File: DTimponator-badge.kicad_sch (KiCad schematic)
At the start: 29 parts, among them J1 AVR-ISP, SW1 SW_SPDT, SW2 SW_Push, SW3 SW_Push, U1 ATtiny84A-SS

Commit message: Changed much to SMD
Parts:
- C1: footprint Capacitor_THT:C_Disc_D5.0mm_W2.5mm_P5.00mm -> Capacitor_SMD:C_1206_3216Metric_Pad1.33x1.80mm_HandSolder
- J1: footprint Connector_IDC:IDC-Header_2x03_P2.54mm_Vertical -> Connector_PinHeader_2.54mm:PinHeader_2x03_P2.54mm_Vertical_SMD
- R1, R2, R3, R4, R5, R6: footprint Resistor_THT:R_Axial_DIN0207_L6.3mm_D2.5mm_P7.62mm_Horizontal -> Resistor_SMD:R_0805_2012Metric_Pad1.20x1.40mm_HandSolder
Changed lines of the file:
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@@
     (property "Reference" "R1" (id 0) (at 41.91 83.6422 90))
     (property "Value" "330" (id 1) (at 41.91 85.9536 90))
-    (property "Footprint" "Resistor_THT:R_Axial_DIN0207_L6.3mm_D2.5mm_P7.62mm_Horizontal" (id 2) (at 41.91 87.122 90)
+    (property "Footprint" "Resistor_SMD:R_0805_2012Metric_Pad1.20x1.40mm_HandSolder" (id 2) (at 41.91 87.122 90)
       (effects (font (size 1.27 1.27)) hide)
     )
@@
     (property "Reference" "R2" (id 0) (at 41.91 109.0422 90))
     (property "Value" "330" (id 1) (at 41.91 111.3536 90))
-    (property "Footprint" "Resistor_THT:R_Axial_DIN0207_L6.3mm_D2.5mm_P7.62mm_Horizontal" (id 2) (at 41.91 112.522 90)
+    (property "Footprint" "Resistor_SMD:R_0805_2012Metric_Pad1.20x1.40mm_HandSolder" (id 2) (at 41.91 112.522 90)
       (effects (font (size 1.27 1.27)) hide)
     )
@@
     (property "Reference" "R3" (id 0) (at 41.91 134.4422 90))
     (property "Value" "330" (id 1) (at 41.91 136.7536 90))
-    (property "Footprint" "Resistor_THT:R_Axial_DIN0207_L6.3mm_D2.5mm_P7.62mm_Horizontal" (id 2) (at 41.91 137.922 90)
+    (property "Footprint" "Resistor_SMD:R_0805_2012Metric_Pad1.20x1.40mm_HandSolder" (id 2) (at 41.91 137.922 90)
       (effects (font (size 1.27 1.27)) hide)
     )
@@
     (property "Reference" "R4" (id 0) (at 41.91 159.8422 90))
     (property "Value" "330" (id 1) (at 41.91 162.1536 90))
-    (property "Footprint" "Resistor_THT:R_Axial_DIN0207_L6.3mm_D2.5mm_P7.62mm_Horizontal" (id 2) (at 41.91 163.322 90)
+    (property "Footprint" "Resistor_SMD:R_0805_2012Metric_Pad1.20x1.40mm_HandSolder" (id 2) (at 41.91 163.322 90)
       (effects (font (size 1.27 1.27)) hide)
     )
@@
       (effects (font (size 1.27 1.27)) (justify right))
     )
-    (property "Footprint" "Connector_IDC:IDC-Header_2x03_P2.54mm_Vertical" (id 2) (at 257.81 54.61 90)
+    (property "Footprint" "Connector_PinHeader_2.54mm:PinHeader_2x03_P2.54mm_Vertical_SMD" (id 2) (at 257.81 54.61 90)
       (effects (font (size 1.27 1.27)) hide)
     )
@@
     (property "Reference" "R5" (id 0) (at 156.21 70.9422 90))
     (property "Value" "10k" (id 1) (at 156.21 73.2536 90))
-    (property "Footprint" "Resistor_THT:R_Axial_DIN0207_L6.3mm_D2.5mm_P7.62mm_Horizontal" (id 2) (at 156.21 74.422 90)
+    (property "Footprint" "Resistor_SMD:R_0805_2012Metric_Pad1.20x1.40mm_HandSolder" (id 2) (at 156.21 74.422 90)
       (effects (font (size 1.27 1.27)) hide)
     )
@@
     (property "Reference" "R6" (id 0) (at 194.31 70.9422 90))
     (property "Value" "10k" (id 1) (at 194.31 73.2536 90))
-    (property "Footprint" "Resistor_THT:R_Axial_DIN0207_L6.3mm_D2.5mm_P7.62mm_Horizontal" (id 2) (at 194.31 74.422 90)
+    (property "Footprint" "Resistor_SMD:R_0805_2012Metric_Pad1.20x1.40mm_HandSolder" (id 2) (at 194.31 74.422 90)
       (effects (font (size 1.27 1.27)) hide)
     )
@@
       (effects (font (size 1.27 1.27)) (justify left))
     )
-    (property "Footprint" "Capacitor_THT:C_Disc_D5.0mm_W2.5mm_P5.00mm" (id 2) (at 73.3552 49.53 0)
+    (property "Footprint" "Capacitor_SMD:C_1206_3216Metric_Pad1.33x1.80mm_HandSolder" (id 2) (at 73.3552 49.53 0)
       (effects (font (size 1.27 1.27)) hide)
     )
@@
     )
     (path "/00000000-0000-0000-0000-0000601b337a"
-      (reference "C1") (unit 1) (value ".1uF") (footprint "Capacitor_THT:C_Disc_D5.0mm_W2.5mm_P5.00mm")
+      (reference "C1") (unit 1) (value ".1uF") (footprint "Capacitor_SMD:C_1206_3216Metric_Pad1.33x1.80mm_HandSolder")
     )
     (path "/00000000-0000-0000-0000-00005fc12c5a"
@@
     )
     (path "/00000000-0000-0000-0000-00005fcd6c92"
-      (reference "J1") (unit 1) (value "AVR-ISP") (footprint "Connector_IDC:IDC-Header_2x03_P2.54mm_Vertical")
+      (reference "J1") (unit 1) (value "AVR-ISP") (footprint "Connector_PinHeader_2.54mm:PinHeader_2x03_P2.54mm_Vertical_SMD")
     )
     (path "/00000000-0000-0000-0000-00005fc55ab2"
-      (reference "R1") (unit 1) (value "330") (footprint "Resistor_THT:R_Axial_DIN0207_L6.3mm_D2.5mm_P7.62mm_Horizontal")
+      (reference "R1") (unit 1) (value "330") (footprint "Resistor_SMD:R_0805_2012Metric_Pad1.20x1.40mm_HandSolder")
     )
     (path "/00000000-0000-0000-0000-00005fc7641b"
-      (reference "R2") (unit 1) (value "330") (footprint "Resistor_THT:R_Axial_DIN0207_L6.3mm_D2.5mm_P7.62mm_Horizontal")
+      (reference "R2") (unit 1) (value "330") (footprint "Resistor_SMD:R_0805_2012Metric_Pad1.20x1.40mm_HandSolder")
     )
     (path "/00000000-0000-0000-0000-00005fc76f9f"
-      (reference "R3") (unit 1) (value "330") (footprint "Resistor_THT:R_Axial_DIN0207_L6.3mm_D2.5mm_P7.62mm_Horizontal")
+      (reference "R3") (unit 1) (value "330") (footprint "Resistor_SMD:R_0805_2012Metric_Pad1.20x1.40mm_HandSolder")
     )
     (path "/00000000-0000-0000-0000-00005fc772c9"
-      (reference "R4") (unit 1) (value "330") (footprint "Resistor_THT:R_Axial_DIN0207_L6.3mm_D2.5mm_P7.62mm_Horizontal")
+      (reference "R4") (unit 1) (value "330") (footprint "Resistor_SMD:R_0805_2012Metric_Pad1.20x1.40mm_HandSolder")
     )
     (path "/00000000-0000-0000-0000-00005fdaba63"
-      (reference "R5") (unit 1) (value "10k") (footprint "Resistor_THT:R_Axial_DIN0207_L6.3mm_D2.5mm_P7.62mm_Horizontal")
+      (reference "R5") (unit 1) (value "10k") (footprint "Resistor_SMD:R_0805_2012Metric_Pad1.20x1.40mm_HandSolder")
     )
     (path "/00000000-0000-0000-0000-00005fdaccd5"
-      (reference "R6") (unit 1) (value "10k") (footprint "Resistor_THT:R_Axial_DIN0207_L6.3mm_D2.5mm_P7.62mm_Horizontal")
+      (reference "R6") (unit 1) (value "10k") (footprint "Resistor_SMD:R_0805_2012Metric_Pad1.20x1.40mm_HandSolder")
     )
     (path "/00000000-0000-0000-0000-00005fcb2142"

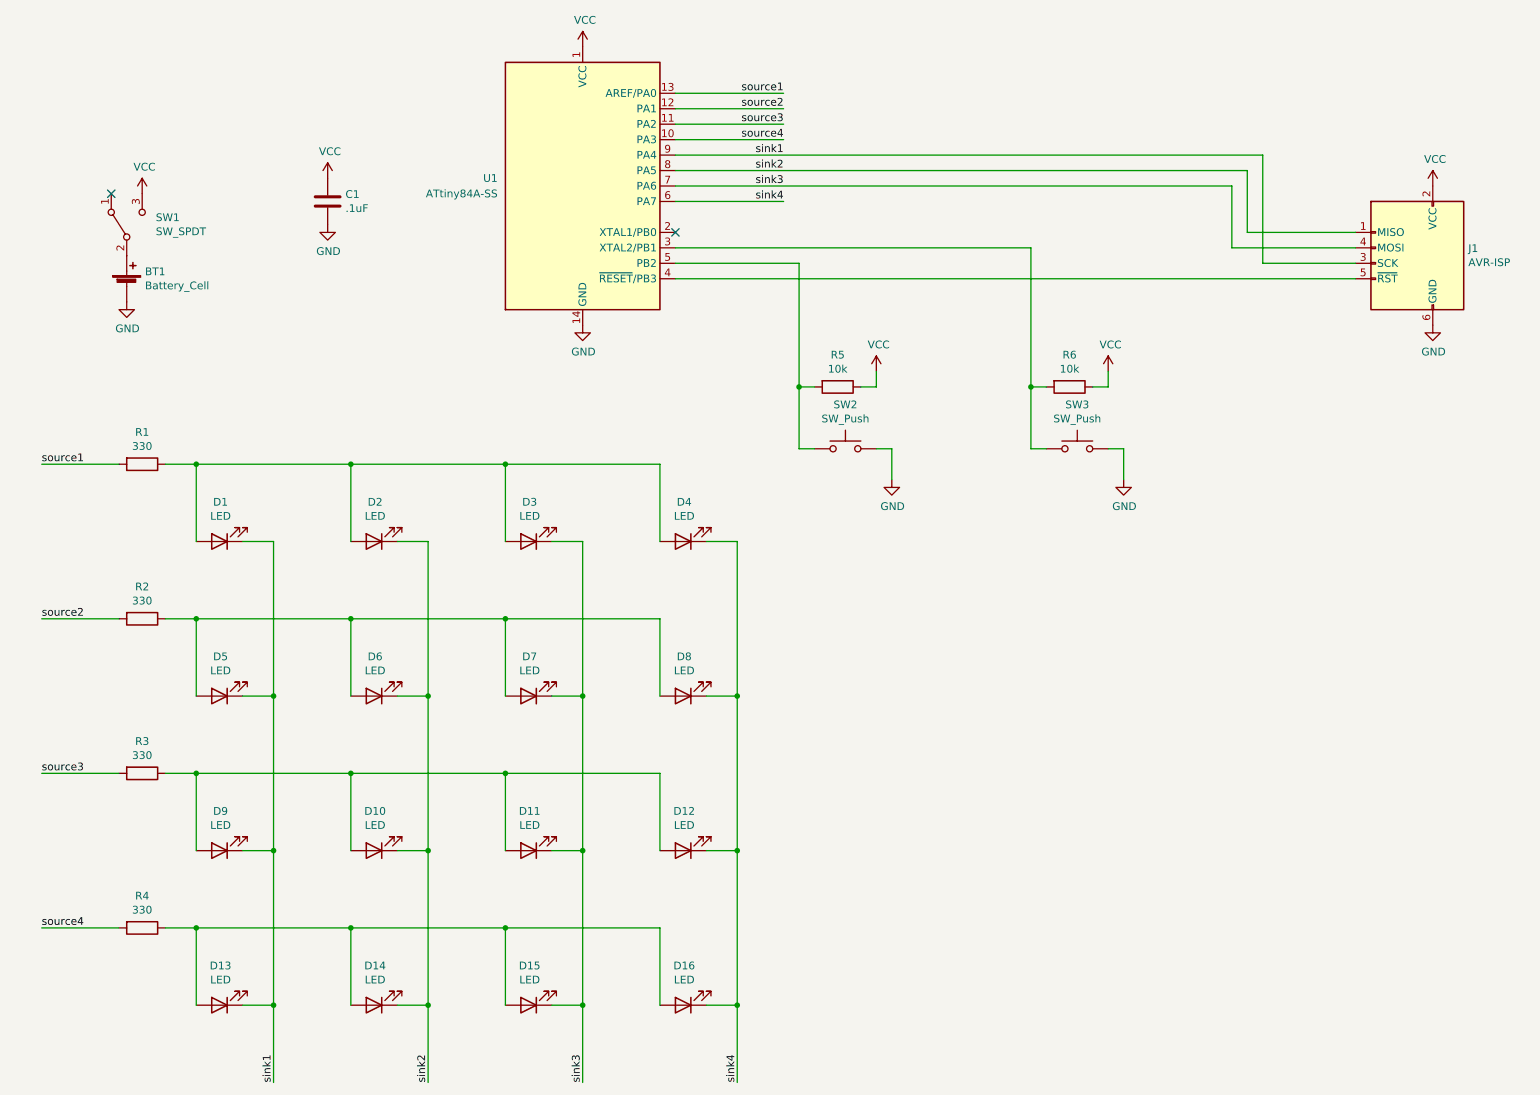
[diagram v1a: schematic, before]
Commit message: Changed to dimmable SMD LEDs
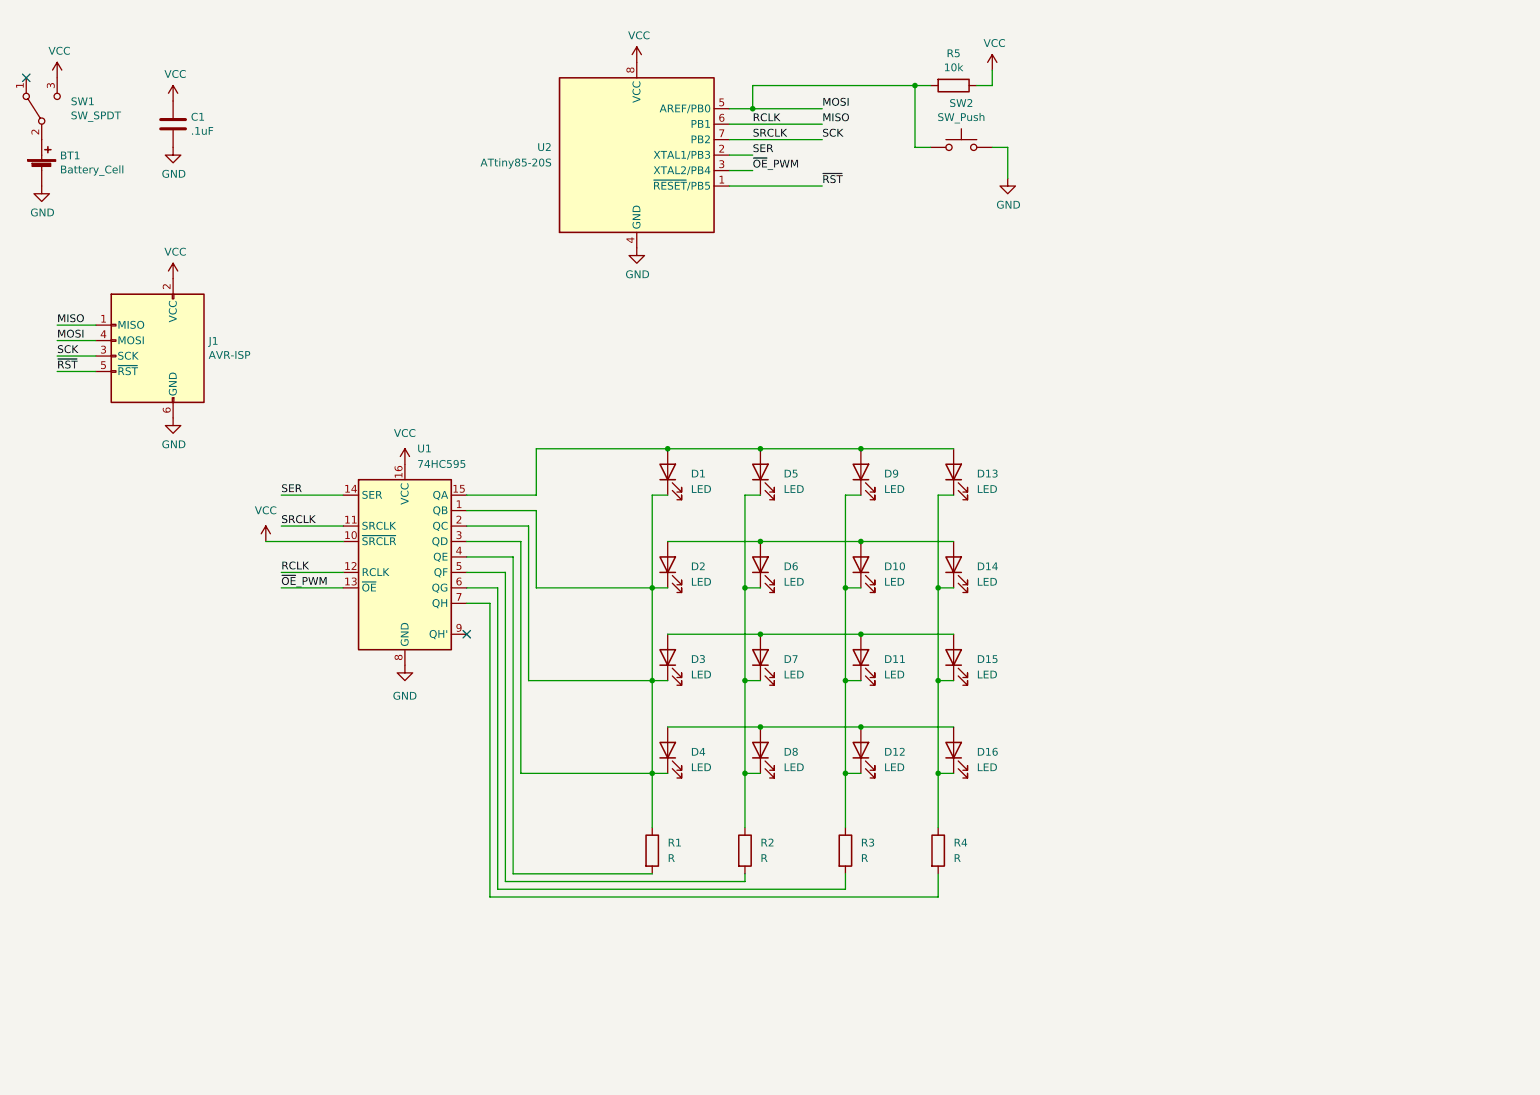
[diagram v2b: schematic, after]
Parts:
- removed R6: 10k, Resistor_SMD:R_0805_2012Metric_Pad1.20x1.40mm_HandSolder, symbol Device:R
- removed SW3: SW_Push, Button_Switch_THT:SW_PUSH_6mm_H5mm, symbol Switch:SW_Push
- removed U1: ATtiny84A-SS, Package_SO:SOIC-14_3.9x8.7mm_P1.27mm, symbol MCU_Microchip_ATtiny:ATtiny84A-SS
- added U1: 74HC595, Package_SO:TSSOP-16_4.4x5mm_P0.65mm, symbol 74xx:74HC595
- added U2: ATtiny85-20S, Package_SO:SOIC-8W_5.3x5.3mm_P1.27mm, symbol MCU_Microchip_ATtiny:ATtiny85-20S
- D1, D10, D11, D12, D13, D14, D15, D16, D2, D3, D4, D5, D6, D7, D8, D9: footprint LED_THT:LED_D5.0mm -> LED_SMD:LED_0603_1608Metric_Pad1.05x0.95mm_HandSolder
- R1, R2, R3, R4: value 330 -> R
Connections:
- net GND: now also U1.8 (GND), U2.4 (GND)
- net VCC: now also U1.10 (~{SRCLR}), U1.16 (VCC), U2.8 (VCC)
- net ~{RST}: now reaches J1.5 (~{RST})
- net ~{RST}: now also U2.1 (~{RESET}/PB5)
- net MOSI: now reaches R5.2, SW2.1
- net MOSI: now also J1.4 (MOSI), U2.5 (AREF/PB0)
- removed net sink1: D1.1 (K), D13.1 (K), D5.1 (K), D9.1 (K), J1.3 (SCK)
- removed net sink2: D10.1 (K), D14.1 (K), D2.1 (K), D6.1 (K), J1.1 (MISO)
- removed net sink3: D11.1 (K), D15.1 (K), D3.1 (K), D7.1 (K), J1.4 (MOSI)
- removed net sink4: D12.1 (K), D16.1 (K), D4.1 (K), D8.1 (K)
- net source1: no longer names the net of R1.2
- net source1: now also U1.4 (QE)
- net source2: no longer names the net of R2.2
- net source2: now also U1.5 (QF)
- net source3: no longer names the net of R3.2
- net source3: now also U1.6 (QG)
- net source4: no longer names the net of R4.2
- net source4: now also U1.7 (QH)
- new net: D5.1 (K), D6.1 (K), D7.1 (K), D8.1 (K), R2.1
- new net: D1.1 (K), D2.1 (K), D3.1 (K), D4.1 (K), R1.1, U1.1 (QB), U1.2 (QC), U1.3 (QD)
- new net: D11.2 (A), D15.2 (A), D3.2 (A), D7.2 (A)
- new net: D10.1 (K), D11.1 (K), D12.1 (K), D9.1 (K), R3.1
- new net: D1.2 (A), D13.2 (A), D5.2 (A), D9.2 (A), U1.15 (QA)
- new net: D13.1 (K), D14.1 (K), D15.1 (K), D16.1 (K), R4.1
- new net: D12.2 (A), D16.2 (A), D4.2 (A), D8.2 (A)
- new net: D10.2 (A), D14.2 (A), D2.2 (A), D6.2 (A)
- new net MISO: J1.1 (MISO), U1.12 (RCLK), U2.6 (PB1)
- new net SCK: J1.3 (SCK), U1.11 (SRCLK), U2.7 (PB2)
- new net SER: U1.14 (SER), U2.2 (XTAL1/PB3)
- new net ~{OE}_PWM: U1.13 (~{OE}), U2.3 (XTAL2/PB4)
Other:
- moved on the sheet: BT1, C1, J1, R5, SW1, SW2

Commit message: Changed from led matrix to led array for increased brightness, routed pcb.
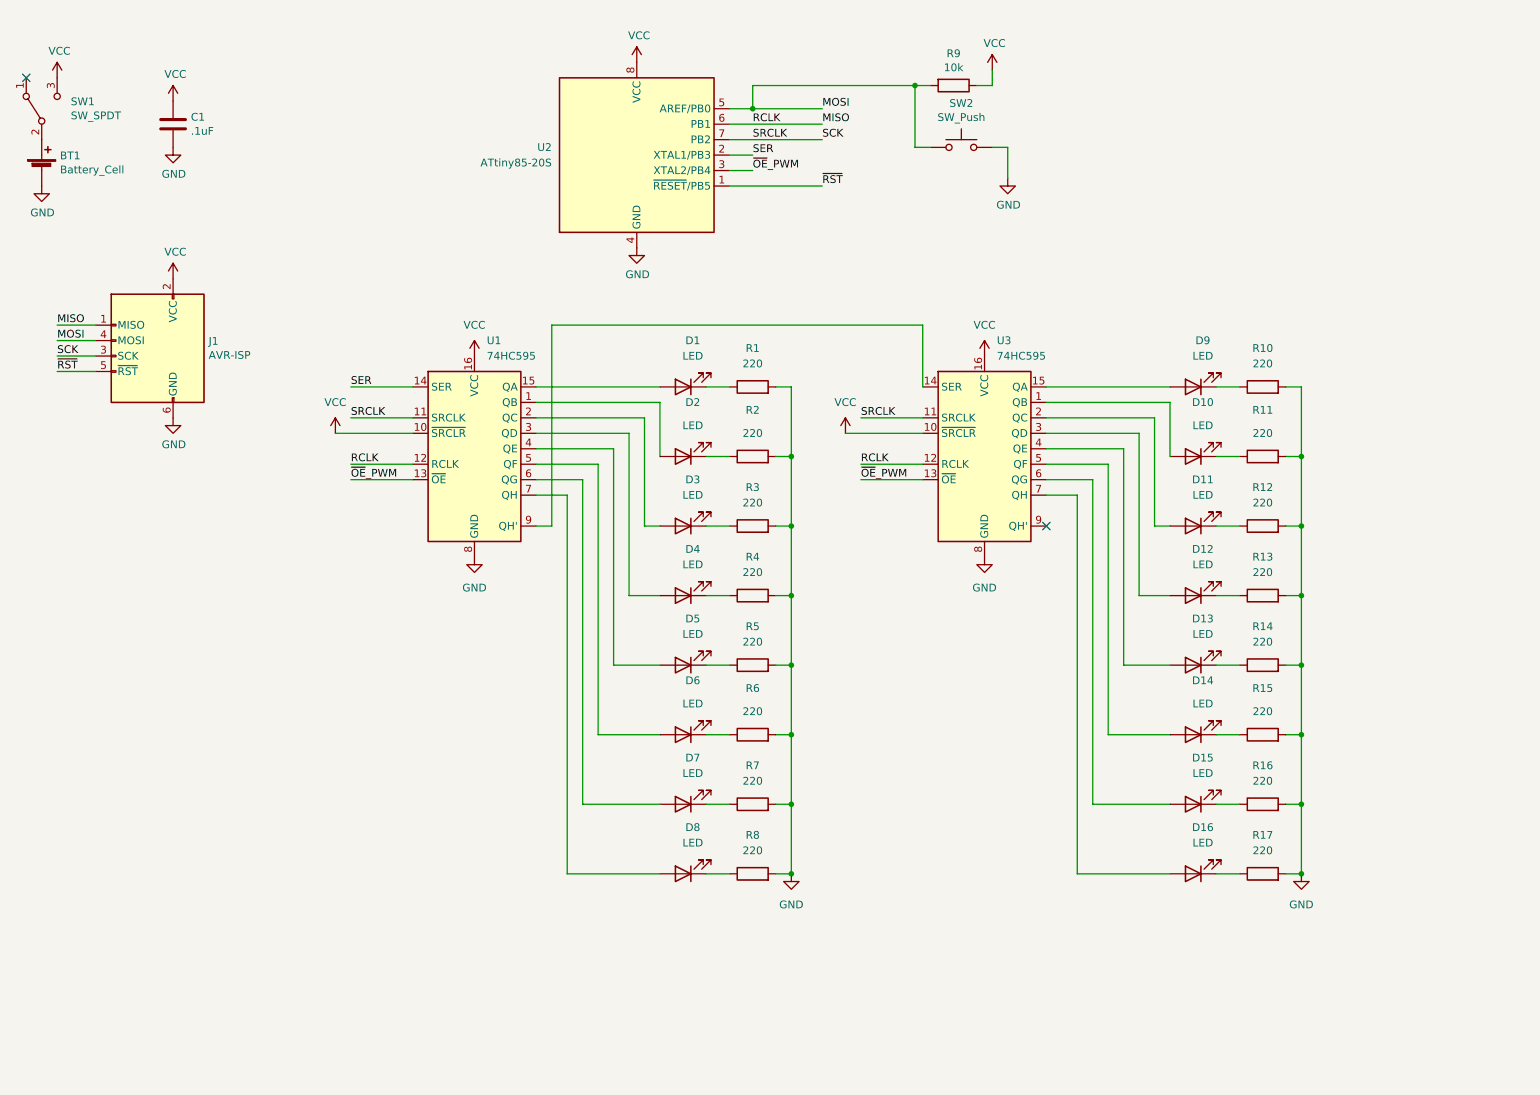
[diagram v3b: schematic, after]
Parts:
- added R10, R11, R12, R13, R14, R15, R16, R17, R5, R6, R7, R8: 220, Resistor_SMD:R_0805_2012Metric_Pad1.20x1.40mm_HandSolder, symbol Device:R
- added U3: 74HC595, Package_SO:TSSOP-16_4.4x5mm_P0.65mm, symbol 74xx:74HC595
- R1, R2, R3, R4: value R -> 220
- renumbered R5 to R9
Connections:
- net GND: now also R1.2, R2.2, R3.2, R4.2, R10.2, R11.2, R12.2, R13.2, R14.2, R15.2, R16.2, R17.2, R5.2, R6.2, R7.2, R8.2, U3.8 (GND)
- net MISO: now also U3.12 (RCLK)
- net SCK: now also U3.11 (SRCLK)
- net VCC: now also U3.10 (~{SRCLR}), U3.16 (VCC)
- net ~{OE}_PWM: now also U3.13 (~{OE})
- net at U1.5 (QF): now also D6.2 (A); no longer R2.2
- net at U1.4 (QE): now also D5.2 (A); no longer R1.2
- net at U1.7 (QH): now also D8.2 (A); no longer R4.2
- net at U1.6 (QG): now also D7.2 (A); no longer R3.2
- net at U1.9 (QH'): now also U3.14 (SER)
- new net: D5.1 (K), R5.1
- new net: D16.1 (K), R17.1
- new net: D16.2 (A), U3.7 (QH)
- new net: D4.1 (K), R4.1
- new net: D4.2 (A), U1.3 (QD)
- new net: D13.1 (K), R14.1
- new net: D13.2 (A), U3.4 (QE)
- new net: D1.1 (K), R1.1
- new net: D11.1 (K), R12.1
- new net: D3.1 (K), R3.1
- new net: D6.1 (K), R6.1
- new net: D15.1 (K), R16.1
- new net: D15.2 (A), U3.6 (QG)
- new net: D1.2 (A), U1.15 (QA)
- new net: D8.1 (K), R8.1
- new net: D2.2 (A), U1.1 (QB)
- new net: D3.2 (A), U1.2 (QC)
- new net: D7.1 (K), R7.1
- new net: D14.1 (K), R15.1
- new net: D9.1 (K), R10.1
- new net: D9.2 (A), U3.15 (QA)
- new net: D11.2 (A), U3.2 (QC)
- new net: D14.2 (A), U3.5 (QF)
- new net: D12.1 (K), R13.1
- new net: D12.2 (A), U3.3 (QD)
- new net: D2.1 (K), R2.1
- new net: D10.2 (A), U3.1 (QB)
- new net: D10.1 (K), R11.1
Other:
- moved on the sheet: U1

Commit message: Made V2
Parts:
- removed SW2: SW_Push, Button_Switch_THT:SW_PUSH_6mm_H5mm, symbol Switch:SW_Push
- BT1: footprint DTimponator-badge:MP000362_CR2032_Holder_THT -> Battery:BatteryHolder_Multicomp_BC-2001_1x2032
- J1: footprint Connector_PinHeader_2.54mm:PinHeader_2x03_P2.54mm_Vertical_SMD -> Connector_PinHeader_2.54mm:PinHeader_2x03_P2.54mm_Horizontal
- SW1: footprint DTimponator-badge:OS102011MA1QN1_SPDT_SlideSwithch_THT -> Button_Switch_THT:SW_E-Switch_EG1224_SPDT_Angled
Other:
- company: (none) -> Dei Taktlause
- moved on the sheet: C1
